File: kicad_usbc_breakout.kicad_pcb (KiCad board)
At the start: 2 copper layers, 6 parts, among them J1 USB_C_Receptacle_USB2.0_16P, J2 Conn_01x01

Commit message: routing for pcb
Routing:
- net VBUS: track 0.00 -> 21.5 mm
- net /CC2: track 0.00 -> 14.1 mm
- net /D+: track 0.00 -> 12.8 mm
- net /D-: track 0.00 -> 12.6 mm
- net /CC1: track 0.00 -> 7.73 mm
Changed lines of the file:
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@@
 		)
 	)
+	(segment
+		(start 122.791373 84.25)
+		(end 122.897 84.25)
+		(width 0.254)
+		(layer "F.Cu")
+		(net 2)
+	)
+	(segment
+		(start 122.897 84.25)
+		(end 130.914 84.25)
+		(width 0.254)
+		(layer "F.Cu")
+		(net 2)
+	)
+	(segment
+		(start 121.941373 85.1)
+		(end 122.791373 84.25)
+		(width 0.254)
+		(layer "F.Cu")
+		(net 2)
+	)
+	(segment
+		(start 121.547 85.1)
+		(end 121.941373 85.1)
+		(width 0.254)
+		(layer "F.Cu")
+		(net 2)
+	)
+	(segment
+		(start 130.914 84.25)
+		(end 133.096 82.068)
+		(width 0.254)
+		(layer "F.Cu")
+		(net 2)
+	)
+	(segment
+		(start 131.328 85.1)
+		(end 133.096 86.868)
+		(width 0.254)
+		(layer "F.Cu")
+		(net 3)
+	)
+	(segment
+		(start 122.897 85.1)
+		(end 131.328 85.1)
+		(width 0.254)
+		(layer "F.Cu")
+		(net 3)
+	)
+	(segment
+		(start 121.715 84.25)
+		(end 122.565 85.1)
+		(width 0.254)
+		(layer "B.Cu")
+		(net 3)
+	)
+	(segment
+		(start 121.547 84.25)
+		(end 121.715 84.25)
+		(width 0.254)
+		(layer "B.Cu")
+		(net 3)
+	)
+	(segment
+		(start 122.565 85.1)
+		(end 122.897 85.1)
+		(width 0.254)
+		(layer "B.Cu")
+		(net 3)
+	)
+	(segment
+		(start 126.238 80.824)
+		(end 129.54 80.824)
+		(width 0.254)
+		(layer "F.Cu")
+		(net 5)
+	)
+	(segment
+		(start 126.212 80.798)
+		(end 126.238 80.824)
+		(width 0.254)
+		(layer "F.Cu")
+		(net 5)
+	)
+	(segment
+		(start 123.382 83.4)
+		(end 125.984 80.798)
+		(width 0.254)
+		(layer "F.Cu")
+		(net 5)
+	)
+	(segment
+		(start 125.984 80.798)
+		(end 126.212 80.798)
+		(width 0.254)
+		(layer "F.Cu")
+		(net 5)
+	)
+	(segment
+		(start 122.897 83.4)
+		(end 123.382 83.4)
+		(width 0.254)
+		(layer "F.Cu")
+		(net 5)
+	)
+	(segment
+		(start 126.264 88.366)
+		(end 129.54 88.366)
+		(width 0.254)
+		(layer "F.Cu")
+		(net 6)
+	)
+	(segment
+		(start 121.053822 85.95)
+		(end 120.39 86.613822)
+		(width 0.254)
+		(layer "F.Cu")
+		(net 6)
+	)
+	(segment
+		(start 126.238 88.392)
+		(end 126.264 88.366)
+		(width 0.254)
+		(layer "F.Cu")
+		(net 6)
+	)
+	(segment
+		(start 120.39 86.613822)
+		(end 120.39 89.402)
+		(width 0.254)
+		(layer "F.Cu")
+		(net 6)
+	)
+	(segment
+		(start 124.587 89.789)
+		(end 125.984 88.392)
+		(width 0.254)
+		(layer "F.Cu")
+		(net 6)
+	)
+	(segment
+		(start 125.984 88.392)
+		(end 126.238 88.392)
+		(width 0.254)
+		(layer "F.Cu")
+		(net 6)
+	)
+	(segment
+		(start 120.777 89.789)
+		(end 124.587 89.789)
+		(width 0.254)
+		(layer "F.Cu")
+		(net 6)
+	)
+	(segment
+		(start 121.547 85.95)
+		(end 121.053822 85.95)
+		(width 0.254)
+		(layer "F.Cu")
+		(net 6)
+	)
+	(segment
+		(start 120.39 89.402)
+		(end 120.777 89.789)
+		(width 0.254)
+		(layer "F.Cu")
+		(net 6)
+	)
+	(segment
+		(start 122.897 86.8)
+		(end 130.361 86.8)
+		(width 0.508)
+		(layer "F.Cu")
+		(net 7)
+	)
+	(segment
+		(start 130.361 86.8)
+		(end 133.096 89.535)
+		(width 0.508)
+		(layer "F.Cu")
+		(net 7)
+	)
+	(segment
+		(start 121.547 82.55)
+		(end 122.897 82.55)
+		(width 0.508)
+		(layer "F.Cu")
+		(net 7)
+	)
+	(segment
+		(start 121.547 86.8)
+		(end 122.897 86.8)
+		(width 0.508)
+		(layer "F.Cu")
+		(net 7)
+	)
+	(segment
+		(start 133.096 89.535)
+		(end 133.096 91.668)
+		(width 0.508)
+		(layer "F.Cu")
+		(net 7)
+	)
+	(segment
+		(start 121.547 82.55)
+		(end 121.053822 82.55)
+		(width 0.508)
+		(layer "B.Cu")
+		(net 7)
+	)
+	(segment
+		(start 121.261768 86.8)
+		(end 121.547 86.8)
+		(width 0.508)
+		(layer "B.Cu")
+		(net 7)
+	)
+	(segment
+		(start 121.053822 82.55)
+		(end 120.74427 82.859552)
+		(width 0.508)
+		(layer "B.Cu")
+		(net 7)
+	)
+	(segment
+		(start 120.74427 82.859552)
+		(end 120.74427 86.282502)
+		(width 0.508)
+		(layer "B.Cu")
+		(net 7)
+	)
+	(segment
+		(start 120.74427 86.282502)
+		(end 121.261768 86.8)
+		(width 0.508)
+		(layer "B.Cu")
+		(net 7)
+	)
 )

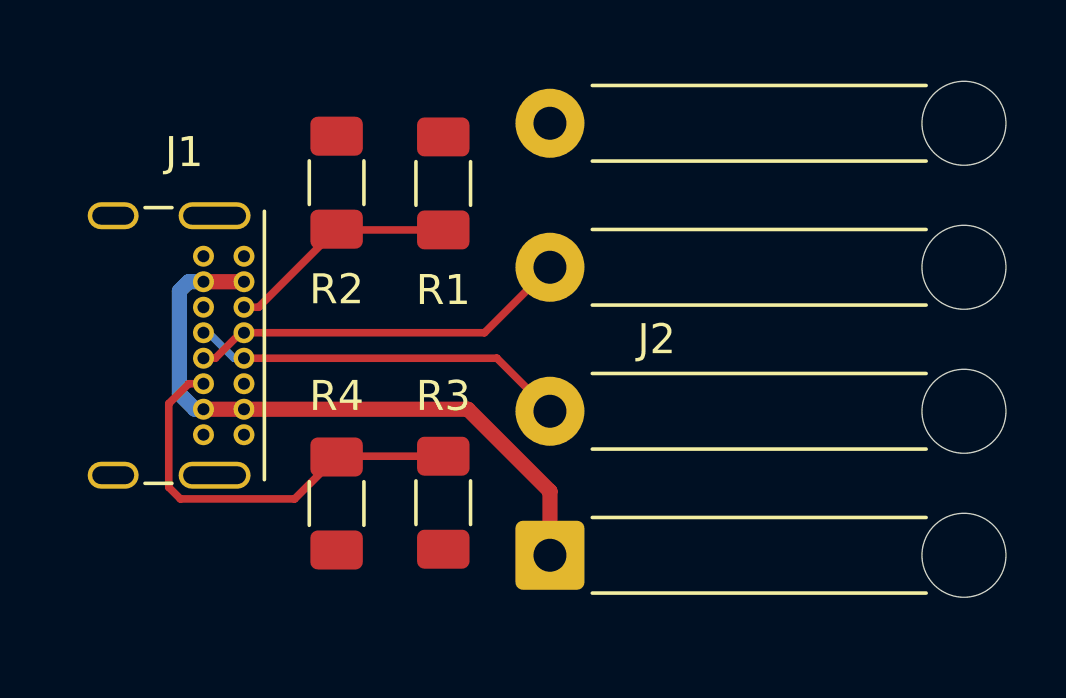
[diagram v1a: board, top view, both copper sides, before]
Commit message: re-placed and routed to make more compact
also changed to 0805 resistors
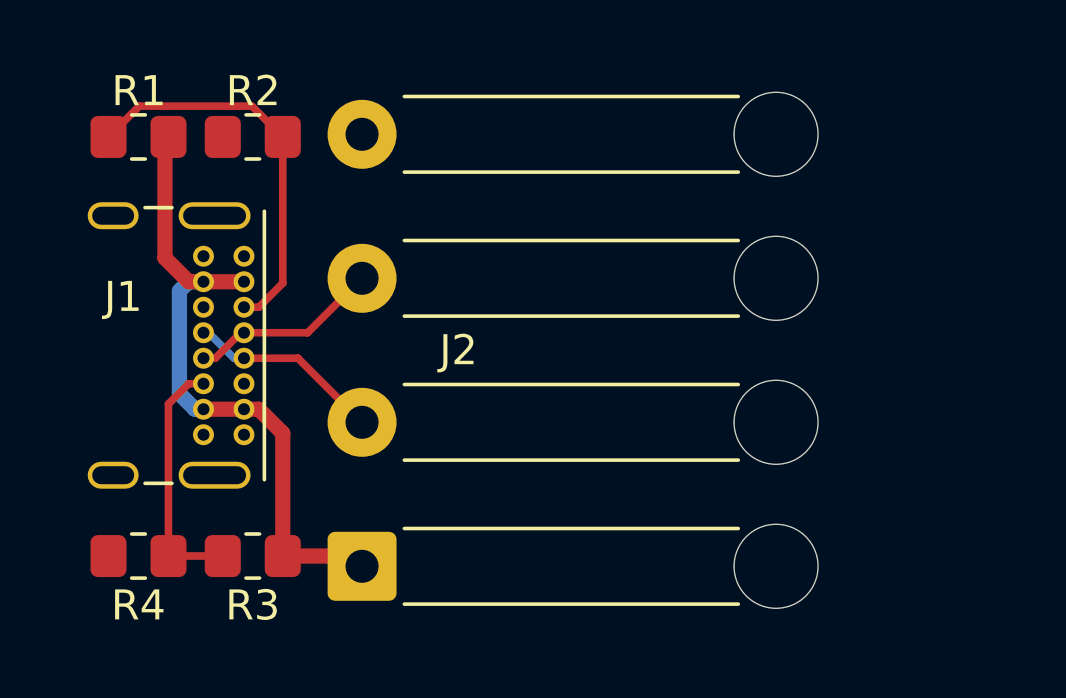
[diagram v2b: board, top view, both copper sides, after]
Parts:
- R1, R2, R3, R4: footprint Resistor_SMD:R_1206_3216Metric_Pad1.30x1.75mm_HandSolder -> Resistor_SMD:R_0805_2012Metric_Pad1.20x1.40mm_HandSolder
- moved R1 10.3 mm to (119.4, 77.7), turned to 180 degrees
- moved R4 6.83 mm to (119.4, 91.7), turned to 180 degrees
- moved R3 6.59 mm to (123.2, 91.7), turned to 180 degrees
- moved J2 6.27 mm to (126.8, 92.0)
- moved R2 3.18 mm to (123.2, 77.7), turned to 180 degrees
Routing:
- net /D+: track 12.8 -> 6.39 mm
- net /D-: track 12.6 -> 6.52 mm
- net /CC2: track 14.1 -> 8.33 mm
- net /CC1: track 7.73 -> 13.2 mm
- net VBUS: track 21.5 -> 22.3 mm

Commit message: made front silk not overlap eachother and be thick enough
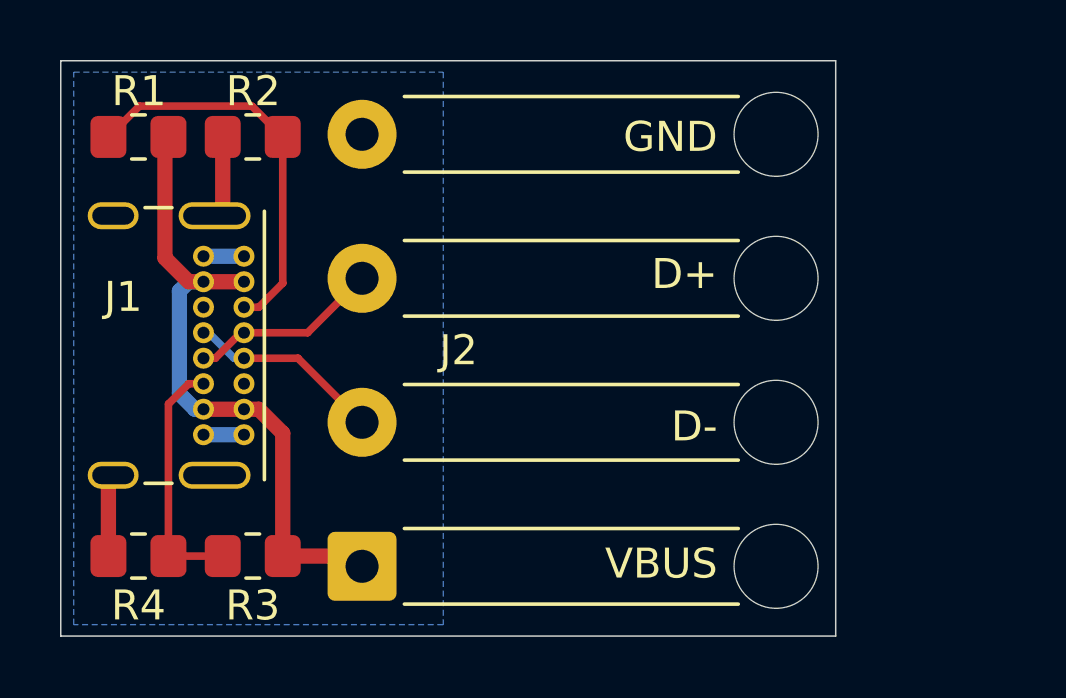
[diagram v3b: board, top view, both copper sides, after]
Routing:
- net GND: track 0.00 -> 8.20 mm
- added copper zone on B.Cu, net GND
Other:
- board outline added: 25.8 x 19.2 mm
- board text added: "D+"
- board text added: "D-"
- board text added: "GND"
- board text added: "USB-C Breakout HugonLabs v1.0 2024-03-29"
- board text added: "VBUS"
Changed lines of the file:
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@@
 		(title "USB-C Breakout")
 		(date "2024-03-29")
+		(rev "1.0")
 		(company "HugonLabs")
 	)
@@
 		)
 	)
+	(gr_rect
+		(start 116.7892 75.184)
+		(end 142.621 94.361)
+		(locked yes)
+		(stroke
+			(width 0.05)
+			(type default)
+		)
+		(fill none)
+		(layer "Edge.Cuts")
+	)
+	(gr_text "VBUS"
+		(at 138.176 91.948 90)
+		(layer "B.SilkS")
+		(effects
+			(font
+				(size 1 1)
+				(thickness 0.127)
+			)
+			(justify bottom mirror)
+		)
+	)
+	(gr_text "USB-C Breakout\nHugonLabs\nv1.0 2024-03-29"
+		(at 133.096 78.232 90)
+		(layer "B.SilkS")
+		(effects
+			(font
+				(size 1 1)
+				(thickness 0.127)
+			)
+			(justify left bottom mirror)
+		)
+	)
+	(gr_text "D-"
+		(at 138.176 87.376 90)
+		(layer "B.SilkS")
+		(effects
+			(font
+				(size 1 1)
+				(thickness 0.127)
+			)
+			(justify bottom mirror)
+		)
+	)
+	(gr_text "D+"
+		(at 138.176 82.296 90)
+		(layer "B.SilkS")
+		(effects
+			(font
+				(size 1 1)
+				(thickness 0.127)
+			)
+			(justify bottom mirror)
+		)
+	)
+	(gr_text "GND"
+		(at 138.176 77.724 90)
+		(layer "B.SilkS")
+		(effects
+			(font
+				(size 1 1)
+				(thickness 0.127)
+			)
+			(justify bottom mirror)
+		)
+	)
+	(gr_text "VBUS"
+		(at 138.684 91.948 0)
+		(layer "F.SilkS")
+		(effects
+			(font
+				(size 1 1)
+				(thickness 0.127)
+			)
+			(justify right)
+		)
+	)
+	(gr_text "D-"
+		(at 138.684 87.376 0)
+		(layer "F.SilkS")
+		(effects
+			(font
+				(size 1 1)
+				(thickness 0.127)
+			)
+			(justify right)
+		)
+	)
+	(gr_text "GND"
+		(at 138.684 77.724 0)
+		(layer "F.SilkS")
+		(effects
+			(font
+				(size 1 1)
+				(thickness 0.127)
+			)
+			(justify right)
+		)
+	)
+	(gr_text "D+"
+		(at 138.684 82.296 0)
+		(layer "F.SilkS")
+		(effects
+			(font
+				(size 1 1)
+				(thickness 0.127)
+			)
+			(justify right)
+		)
+	)
+	(segment
+		(start 122.19 77.724)
+		(end 122.19 80.077)
+		(width 0.508)
+		(layer "F.Cu")
+		(net 1)
+	)
+	(segment
+		(start 118.38 91.694)
+		(end 118.38 89.157)
+		(width 0.508)
+		(layer "F.Cu")
+		(net 1)
+	)
+	(segment
+		(start 122.19 80.077)
+		(end 121.917 80.35)
+		(width 0.508)
+		(layer "F.Cu")
+		(net 1)
+	)
+	(segment
+		(start 118.38 89.157)
+		(end 118.537 89)
+		(width 0.508)
+		(layer "F.Cu")
+		(net 1)
+	)
+	(segment
+		(start 121.547 87.65)
+		(end 122.897 87.65)
+		(width 0.508)
+		(layer "B.Cu")
+		(net 1)
+	)
+	(segment
+		(start 121.547 81.7)
+		(end 122.897 81.7)
+		(width 0.508)
+		(layer "B.Cu")
+		(net 1)
+	)
 	(segment
 		(start 125.019 84.25)
@@
 		(net 7)
 	)
+	(zone
+		(net 1)
+		(net_name "GND")
+		(layer "B.Cu")
+		(name "gnd_plane")
+		(hatch edge 0.5)
+		(connect_pads
+			(clearance 0.5)
+		)
+		(min_thickness 0.25)
+		(filled_areas_thickness no)
+		(fill yes
+			(thermal_gap 0.5)
+			(thermal_bridge_width 0.5)
+		)
+		(polygon
+			(pts
+				(xy 117.221 75.565) (xy 129.54 75.565) (xy 129.54 93.98) (xy 117.221 93.98)
+			)
+		)
+	)
 	(generated

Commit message: switched around wires so that gnd and vbus are next to eachother
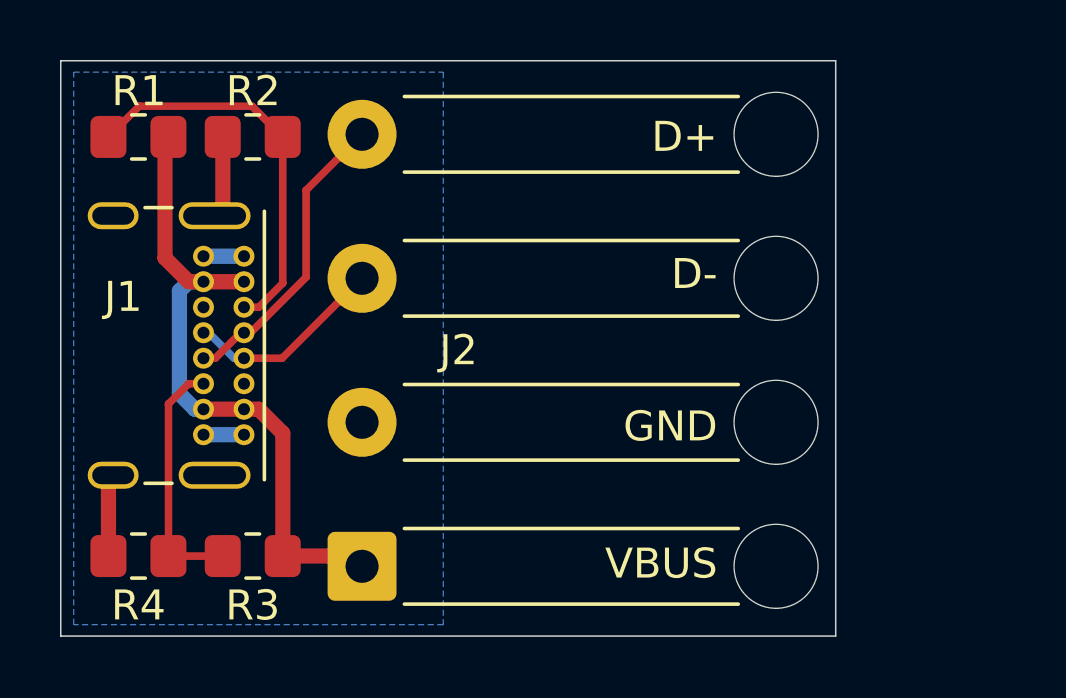
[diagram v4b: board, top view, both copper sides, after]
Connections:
- J2 pad 2: /D- -> GND
- J2 pad 3: /D+ -> /D-
- J2 pad 4: GND -> /D+
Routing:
- net /D+: track 6.39 -> 10.1 mm
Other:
- board text added: "USB-C Breakout HugonLabs v1.1 2024-03-30"
- board text removed: "USB-C Breakout HugonLabs v1.0 2024-03-29"
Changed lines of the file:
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@@
 	(title_block
 		(title "USB-C Breakout")
-		(date "2024-03-29")
-		(rev "1.0")
+		(date "2024-03-30")
+		(rev "1.1")
 		(company "HugonLabs")
 	)
@@
 			(layers "*.Cu" "*.Mask")
 			(remove_unused_layers no)
-			(net 3 "/D-")
+			(net 1 "GND")
 			(pinfunction "Pin_2")
 			(pintype "passive")
@@
 			(layers "*.Cu" "*.Mask")
 			(remove_unused_layers no)
-			(net 2 "/D+")
+			(net 3 "/D-")
 			(pinfunction "Pin_3")
 			(pintype "passive")
@@
 			(layers "*.Cu" "*.Mask")
 			(remove_unused_layers no)
-			(net 1 "GND")
+			(net 2 "/D+")
 			(pinfunction "Pin_4")
 			(pintype "passive")
@@
 		)
 	)
-	(gr_text "USB-C Breakout\nHugonLabs\nv1.0 2024-03-29"
+	(gr_text "USB-C Breakout\nHugonLabs\nv1.1 2024-03-30"
 		(at 133.096 78.232 90)
 		(layer "B.SilkS")
@@
 	)
 	(gr_text "D-"
-		(at 138.176 87.376 90)
+		(at 138.176 82.804 90)
 		(layer "B.SilkS")
 		(effects
@@
 	)
 	(gr_text "D+"
-		(at 138.176 82.296 90)
+		(at 138.176 77.724 90)
 		(layer "B.SilkS")
 		(effects
@@
 	)
 	(gr_text "GND"
-		(at 138.176 77.724 90)
+		(at 138.176 87.376 90)
 		(layer "B.SilkS")
 		(effects
@@
 	)
 	(gr_text "D-"
+		(at 138.684 82.296 0)
+		(layer "F.SilkS")
+		(effects
+			(font
+				(size 1 1)
+				(thickness 0.127)
+			)
+			(justify right)
+		)
+	)
+	(gr_text "GND"
 		(at 138.684 87.376 0)
 		(layer "F.SilkS")
@@
 		)
 	)
-	(gr_text "GND"
+	(gr_text "D+"
 		(at 138.684 77.724 0)
 		(layer "F.SilkS")
@@
 		)
 	)
-	(gr_text "D+"
-		(at 138.684 82.296 0)
-		(layer "F.SilkS")
-		(effects
-			(font
-				(size 1 1)
-				(thickness 0.127)
-			)
-			(justify right)
-		)
-	)
 	(segment
 		(start 122.19 77.724)
@@
 	)
 	(segment
-		(start 125.019 84.25)
-		(end 126.833 82.436)
+		(start 124.968 79.501)
+		(end 126.833 77.636)
 		(width 0.254)
 		(layer "F.Cu")
@@
 	)
 	(segment
+		(start 124.968 82.396914)
+		(end 124.968 79.501)
+		(width 0.254)
+		(layer "F.Cu")
+		(net 2)
+	)
+	(segment
 		(start 122.897 84.25)
-		(end 125.019 84.25)
+		(end 123.114914 84.25)
 		(width 0.254)
 		(layer "F.Cu")
@@
 	)
 	(segment
+		(start 123.114914 84.25)
+		(end 124.968 82.396914)
+		(width 0.254)
+		(layer "F.Cu")
+		(net 2)
+	)
+	(segment
 		(start 121.547 85.1)
 		(end 121.941373 85.1)
@@
 	(segment
 		(start 122.897 85.1)
-		(end 124.697 85.1)
+		(end 124.169 85.1)
 		(width 0.254)
 		(layer "F.Cu")
@@
 	)
 	(segment
-		(start 124.697 85.1)
-		(end 126.833 87.236)
+		(start 124.169 85.1)
+		(end 126.833 82.436)
 		(width 0.254)
 		(layer "F.Cu")
